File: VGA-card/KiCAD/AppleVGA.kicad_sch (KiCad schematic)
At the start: 27 parts, among them U1 74LVC245, U2 74LVC245, U3 74LVC245, U4 74LS07, U5 UA78M33CKCS, U6 Pico

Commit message: KiCAD schematics updated
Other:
- title: Apple II VGA Card -> MPF-II VGA Card
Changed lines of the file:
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@@
   (paper "A4")
   (title_block
-    (title "Apple II VGA Card")
+    (title "MPF-II VGA Card")
     (date "2021-12-13")
     (rev "A")
     (comment 1 "Licensed under CERN-OHL-P V2.0 (https://ohwr.org/cern_ohl_p_v2.txt)")
     (comment 2 "Copyright (c) 2021-2022 Mark Aikens")
+    (comment 3 "Modified for MPF-II: The Random DIY")
   )
   (junction (at 38.1 189.23) (diameter 0) (color 0 0 0 0)

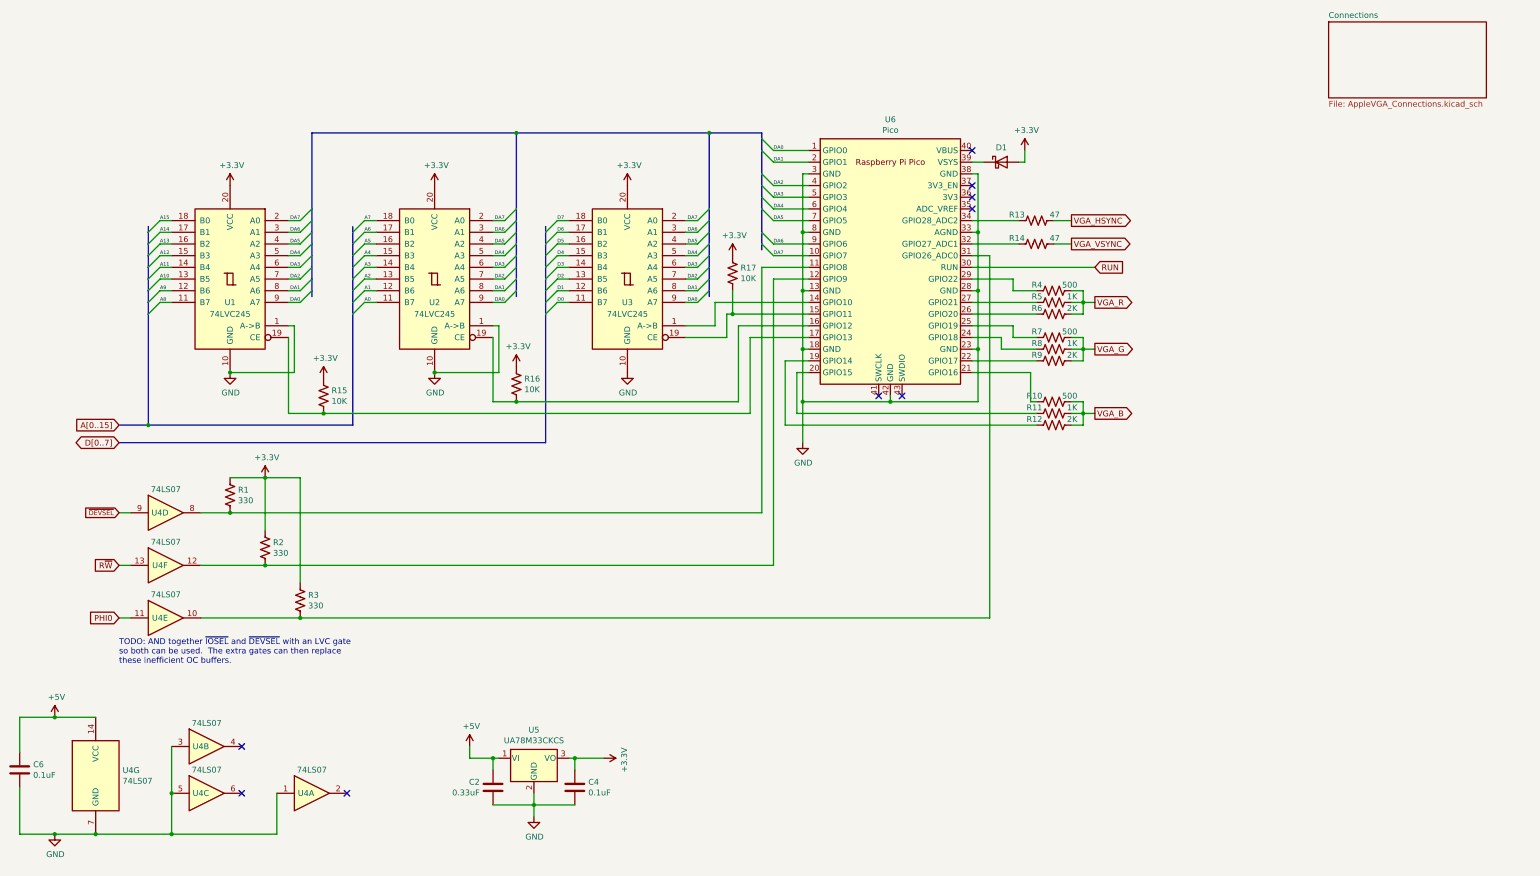
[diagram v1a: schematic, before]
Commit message: KiCAD ERC errors have been fixed
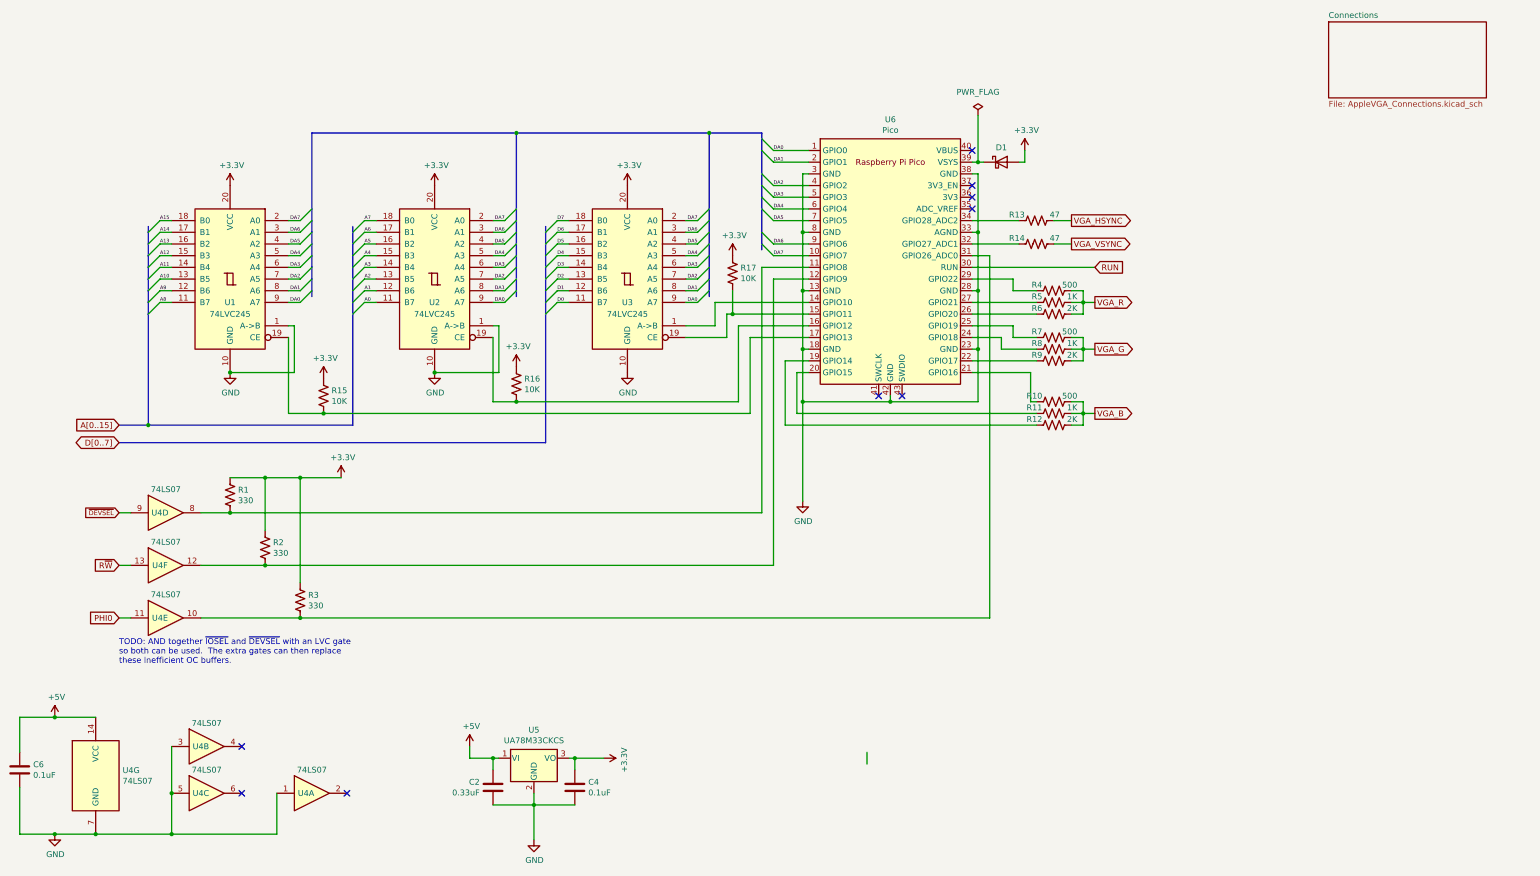
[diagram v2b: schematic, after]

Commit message: KiCAD error fixes
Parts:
- U6: symbol AppleVGA-rescue:Pico-MCU_RaspberryPi_and_Boards -> MCU_RaspberryPi_and_Boards:Pico
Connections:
- net +3V3 renamed +3.3V
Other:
- title: MPF-II VGA Card -> Apple II VGA Card
